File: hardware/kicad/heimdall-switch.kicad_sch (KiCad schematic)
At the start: 27 parts, among them J1 SWD, J2 LOAD_OUT, K1 Relay_SPST_Latching_2coil, Q1 Q_NMOS_GSD, Q2 Q_NMOS_GSD, Q3 Q_PMOS_GSD, SW1 SW_Push, U1 BT832, U2 TPS629206, Y1 32.768kHz

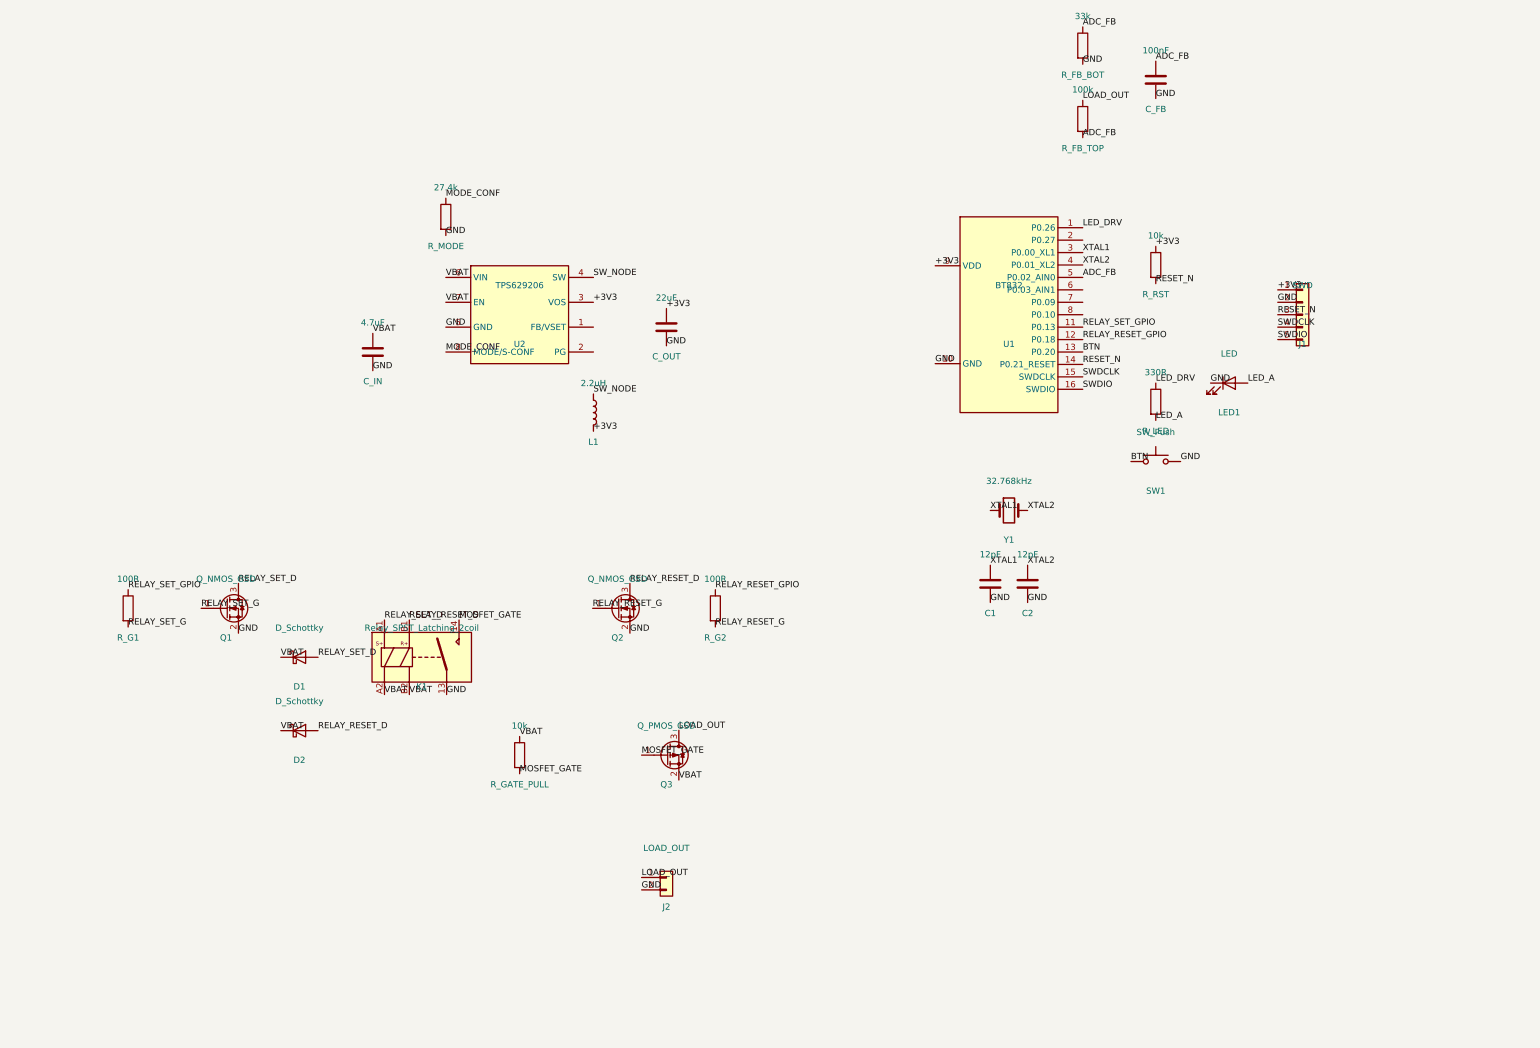
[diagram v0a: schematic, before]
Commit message: Replace latching relay with fail-on MOSFET switch; add flash persistence
Switching: drop the latching relay (no coils/mechanical parts) in favour
of a single high-side P-FET whose hardware default is ON — the MCU must
actively hold the output OFF, so any control-side failure (dead MCU,
reset, brownout, regulator, firmware hang) leaves the load powered.
Slow gate turn-on bridges MCU boot; watchdog is mandatory.

Adds a P-FET ideal-diode reverse polarity stage at the battery input,
covering the node and the load.

State now survives power loss via flash (Jeti SPS-20 approach):
append-only two-page log of {counter, state} per state change, ~10M
changes of endurance, no erase in the command path, verify-on-write
fallback so worn flash never bricks the switch. New persistence.md.

Protocol open items: 8-bit key check byte is forgeable (replace with a
truncated AES-CMAC), 8-bit counter wraps.

Docs: power budget for a 1500mAh 2S LiFePO4 pack (~34uA OFF, ~4 years
shelf), SWD header pinout, BT832 DC/DC + optional 32kHz crystal,
component selection open items.

Schematic: wired KiCad 10 schematic with power symbols/PWR_FLAGs, the
fail-on stage and reverse polarity protection; BT832/TPS629206 symbol
pins moved onto the 2.54mm grid; layout tidied (no overlapping text, no
crossing SWD wires). ERC: 0 errors, 0 warnings. The .kicad_sch is now
the source of truth — the generator scripts are retired.

Co-Authored-By: Claude Opus 5.5 <noreply@anthropic.com>
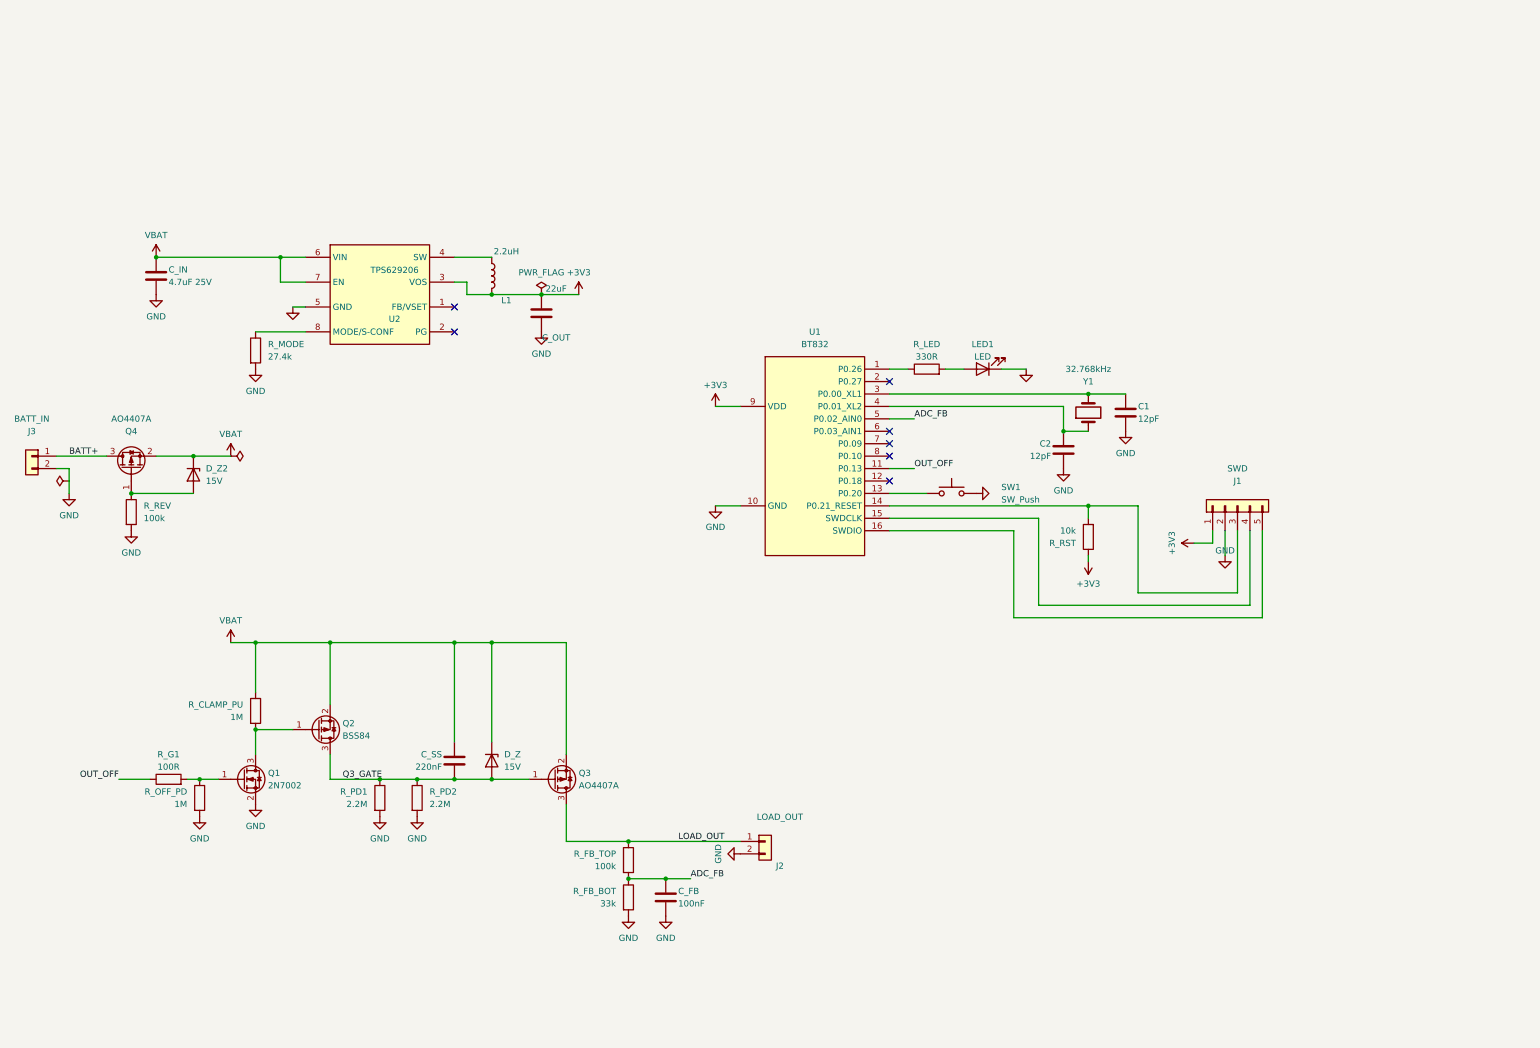
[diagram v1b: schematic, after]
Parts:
- removed D1, D2: D_Schottky, symbol Device:D_Schottky
- removed K1: Relay_SPST_Latching_2coil, symbol Relay:Relay_SPST_Latching_2coil
- removed Q2: Q_NMOS_GSD, symbol Transistor_FET:Q_NMOS_GSD
- removed R_G2: 100R, symbol Device:R
- removed R_GATE_PULL: 10k, symbol Device:R
- added C_SS: 220nF, symbol Device:C
- added D_Z, D_Z2: 15V, symbol Device:D_Zener
- added J3: BATT_IN, symbol Connector_Generic:Conn_01x02
- added Q2: BSS84, symbol Transistor_FET:Q_PMOS_GSD
- added Q4: AO4407A, symbol Transistor_FET:Q_PMOS_GSD
- added R_CLAMP_PU, R_OFF_PD: 1M, symbol Device:R
- added R_PD1, R_PD2: 2.2M, symbol Device:R
- added R_REV: 100k, symbol Device:R
- C_IN: value 4.7uF -> 4.7uF 25V
- Q1: value Q_NMOS_GSD -> 2N7002
- Q3: value Q_PMOS_GSD -> AO4407A
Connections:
- net GND: now also J3.2 (Pin_2), R_OFF_PD.2, R_PD1.2, R_PD2.2, R_REV.2
- net VBAT: now also C_SS.1, D_Z.1 (K), D_Z2.1 (K), Q2.2 (S), Q4.2 (S), R_CLAMP_PU.1
- net BTN: no longer names the net of SW1.1, U1.13 (P0.20)
- net LED_A: no longer names the net of LED1.2 (A), R_LED.2
- net LED_DRV: no longer names the net of R_LED.1, U1.1 (P0.26)
- net MODE_CONF: no longer names the net of R_MODE.1, U2.8 (MODE/S-CONF)
- net MOSFET_GATE renamed Q3_GATE
- net Q3_GATE: now also C_SS.2, D_Z.2 (A), Q2.3 (D), R_PD1.1, R_PD2.1
- net RELAY_RESET_GPIO: no longer names the net of U1.12 (P0.18)
- net RELAY_SET_D: no longer names the net of Q1.3 (D)
- net RELAY_SET_D: now also Q2.1 (G), R_CLAMP_PU.2
- net RELAY_SET_G: no longer names the net of Q1.1 (G), R_G1.2
- net RELAY_SET_G: now also R_OFF_PD.1
- net RELAY_SET_GPIO renamed OUT_OFF
- net RESET_N: no longer names the net of J1.3 (Pin_3), R_RST.2, U1.14 (P0.21_RESET)
- net SWDCLK: no longer names the net of J1.4 (Pin_4), U1.15 (SWDCLK)
- net SWDIO: no longer names the net of J1.5 (Pin_5), U1.16 (SWDIO)
- net SW_NODE: no longer names the net of L1.1, U2.4 (SW)
- net XTAL1: no longer names the net of C1.1, U1.3 (P0.00_XL1)
- net XTAL1: now also Y1.2; no longer Y1.1
- net XTAL2: no longer names the net of C2.1, U1.4 (P0.01_XL2)
- net XTAL2: now also Y1.1; no longer Y1.2
- new net: D_Z2.2 (A), Q4.1 (G), R_REV.1
- new net BATT+: J3.1 (Pin_1), Q4.3 (D)
- no-connect marks 0 -> 7

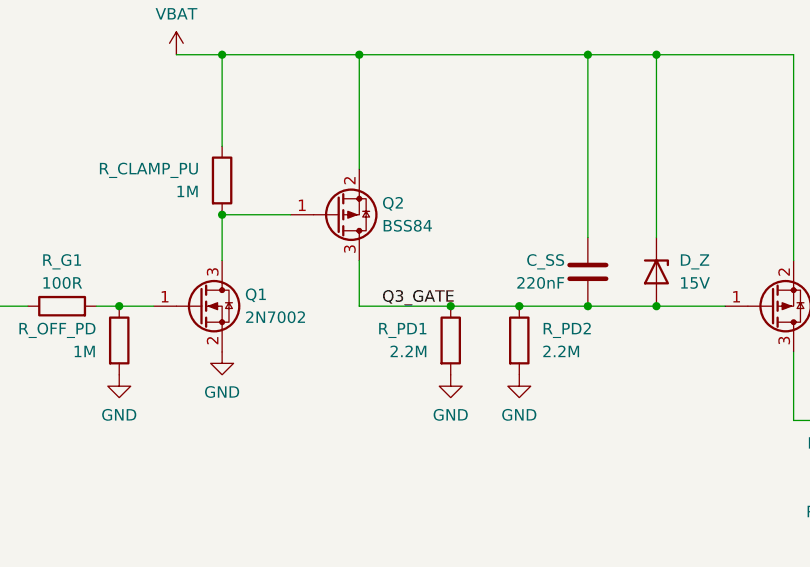
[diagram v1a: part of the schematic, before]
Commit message: Select switching FETs, add R_LIM; document assembly approach
- Q3/Q4: AOS AO4407A (SO-8, C16072). Not specified at -4.5V, but the gate
  always sees the full pack voltage (>=~5V on 2S), where it is <=17mOhm.
  AONR21357 (DFN 3x3) noted as the upgrade for a shrunk board.
- Q1: AO3400A (C20917), logic-level for the 3.3V GPIO drive.
- Q2: Nexperia BSS84 (C493579), high threshold + <=100nA leakage for
  fail-on margin; leakage chain analysed, bench check documented.
- R_LIM 100R between Q2 drain and Q3 gate caps the C_SS discharge spike
  through Q2 at turn-off (~1A -> ~0.1A).
- Assembly: bare JLCPCB boards with leaded HASL, LCSC parts, hand/hot-air
  assembly with Sn63/Pb37, no 0402.

Co-Authored-By: Claude Opus 5.5 <noreply@anthropic.com>
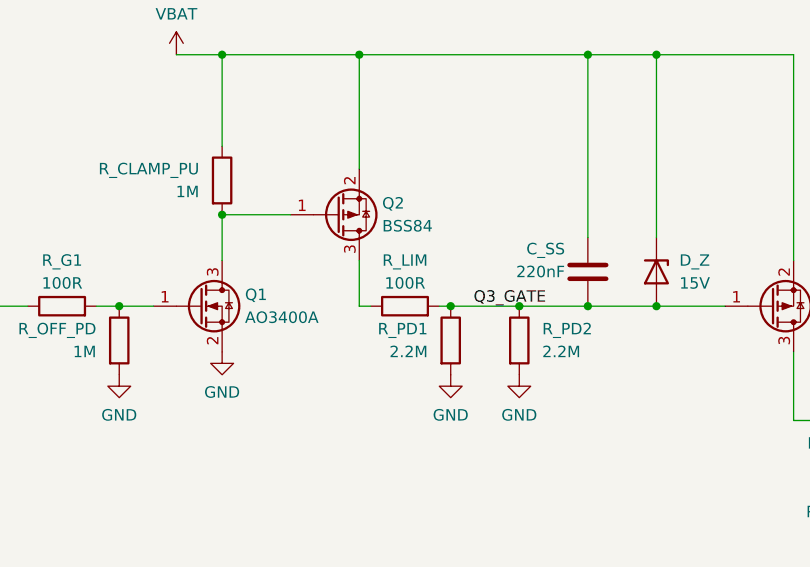
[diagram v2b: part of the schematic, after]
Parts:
- added R_LIM: 100R, symbol Device:R
- Q1: value 2N7002 -> AO3400A
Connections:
- net Q3_GATE: now also R_LIM.2; no longer Q2.3 (D)
- new net: Q2.3 (D), R_LIM.1

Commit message: Select remaining components; add UI breakout and BT832 decoupling
- BOM section in hardware.md with LCSC numbers; hidden LCSC field on
  every schematic part for BOM export
- D_Z/D_Z2 15V -> 18V MMSZ5248B (lower leakage at 12.6V)
- C_SS 50V 0805, C_IN 10uF 50V 1206, C1/C2 18pF for the 12.5pF FC-135
- BT832 VDD decoupling C_VDD1 4.7uF + C_VDD2 100nF
- Status LED is now a 5mm THT high-intensity red; LED1/SW1 moved to
  their own block with J4 breakout (LED_A/BTN/GND) for a daughter
  board, plus R_BTN 1k series ESD protection on P0.20
- Open items: hot-plug ringing on 3S, J1 footprint

Co-Authored-By: Claude Opus 5.5 <noreply@anthropic.com>
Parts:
- added C_VDD1: 4.7uF, symbol Device:C
- added C_VDD2: 100nF, symbol Device:C
- added J4: UI_BREAKOUT, symbol Connector_Generic:Conn_01x03
- added R_BTN: 1k, symbol Device:R
- C1, C2: value 12pF -> 18pF; LCSC (none) -> C1647
- C_FB: LCSC (none) -> C14663
- C_IN: value 4.7uF 25V -> 10uF 50V; LCSC (none) -> C13585
- C_OUT: LCSC (none) -> C45783
- C_SS: value 220nF -> 220nF 50V; LCSC (none) -> C5378
- D_Z, D_Z2: value 15V -> 18V; LCSC (none) -> C2127
- L1: LCSC (none) -> C237482
- LED1: value LED -> Red 5mm; LCSC (none) -> C7470729
- Q1: LCSC (none) -> C20917
- Q2: LCSC (none) -> C493579
- Q3, Q4: LCSC (none) -> C16072
- R_CLAMP_PU, R_OFF_PD: LCSC (none) -> C22935
- R_FB_BOT: LCSC (none) -> C4216
- R_FB_TOP, R_REV: LCSC (none) -> C25803
- R_G1, R_LIM: LCSC (none) -> C22775
- R_LED: LCSC (none) -> C23138
- R_MODE: LCSC (none) -> C22964
- R_PD1, R_PD2: LCSC (none) -> C22938
- R_RST: LCSC (none) -> C25804
- SW1: value SW_Push -> KSC221J; LCSC (none) -> C221726
- U2: LCSC (none) -> C5219292
- Y1: LCSC (none) -> C32346
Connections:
- net +3V3: now also C_VDD1.1, C_VDD2.1
- net GND: now also C_VDD1.2, C_VDD2.2, J4.3 (Pin_3)
- net LED_A: now reaches LED1.2 (A), R_LED.2
- net LED_A: now also J4.1 (Pin_1)
- net at SW1.1: now also J4.2 (Pin_2), R_BTN.2; no longer U1.13 (P0.20)
- new net BTN: R_BTN.1, U1.13 (P0.20)
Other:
- note added: "Status LED + button: fit LED1/SW1 here, or leave them unfitted and wire J4 to a daughter board"

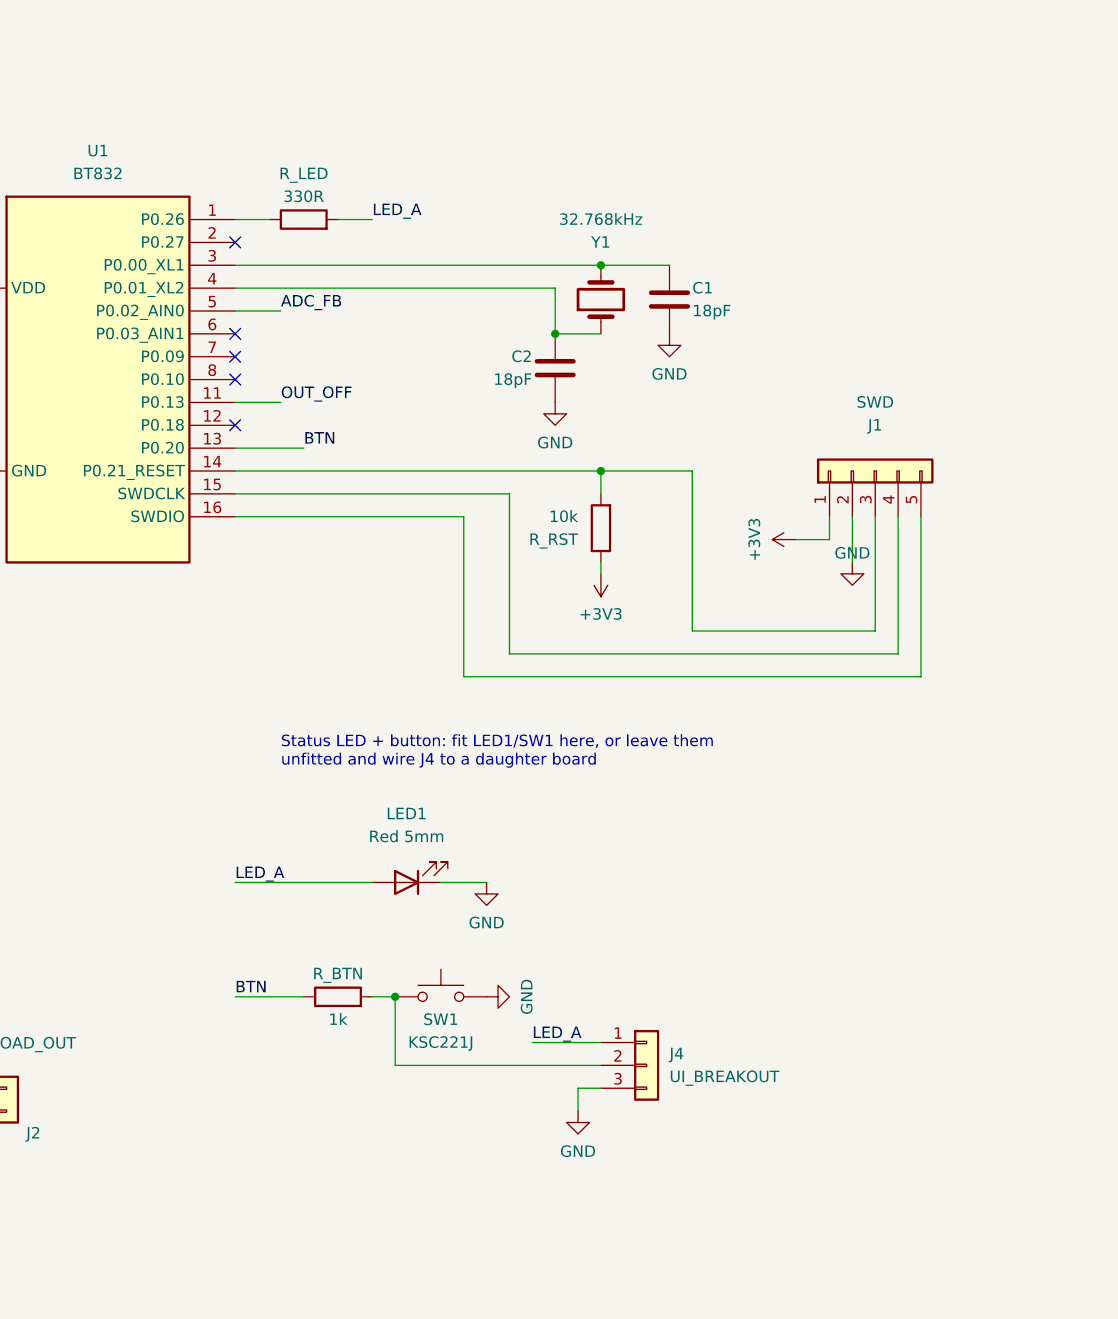
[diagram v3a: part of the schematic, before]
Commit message: Status LED: 3mm high-intensity green driven from VBAT
Sunlight visibility through a 3mm hull hole needs an InGaN LED (~3.2V
forward), which the 3.3V rail can't drive. LED1 is now an Everlight
204-10SUGC (3.2cd, 20deg, water clear) fed from VBAT through R_LED
(680R 1206) and switched low-side by Q5 (AO3400A) on P0.26, with a 1M
gate pull-down. R_LED sits ahead of J4 so a shorted daughter-board wire
stays current-limited. J4 is now 4 pads: LED_A / LED_K / BTN / GND.

Co-Authored-By: Claude Opus 5.5 <noreply@anthropic.com>
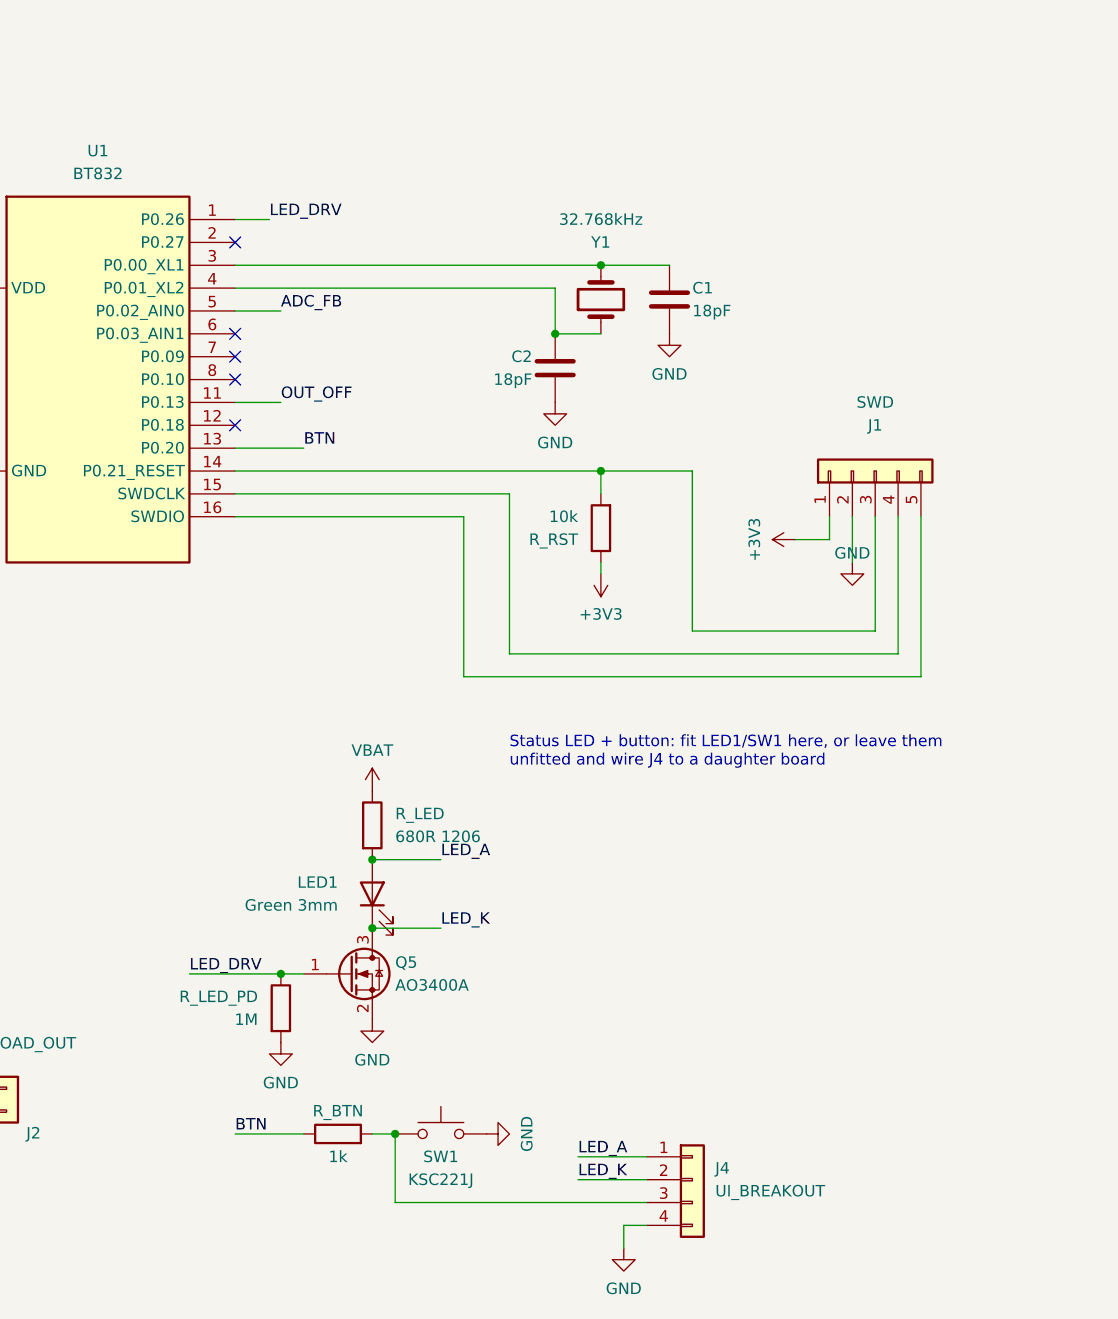
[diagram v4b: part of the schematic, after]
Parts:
- removed J4: UI_BREAKOUT, symbol Connector_Generic:Conn_01x03
- added J4: UI_BREAKOUT, symbol Connector_Generic:Conn_01x04
- added Q5: AO3400A, symbol Transistor_FET:Q_NMOS_GSD
- added R_LED_PD: 1M, symbol Device:R
- LED1: value Red 5mm -> Green 3mm; LCSC C7470729 -> C414645
- R_LED: value 330R -> 680R 1206; LCSC C23138 -> C17975
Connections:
- net GND: now also J4.4 (Pin_4), Q5.2 (S), R_LED_PD.2; no longer LED1.1 (K)
- net LED_A: now also J4.1 (Pin_1)
- net VBAT: now also R_LED.1
- net LED_DRV: now reaches U1.1 (P0.26)
- net LED_DRV: now also Q5.1 (G), R_LED_PD.1; no longer R_LED.1
- net at R_BTN.2, SW1.1: now also J4.3 (Pin_3)
- new net LED_K: J4.2 (Pin_2), LED1.1 (K), Q5.3 (D)
